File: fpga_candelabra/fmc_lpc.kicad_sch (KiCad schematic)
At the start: 2 parts, among them J5 Samtec_ASP-134603-01

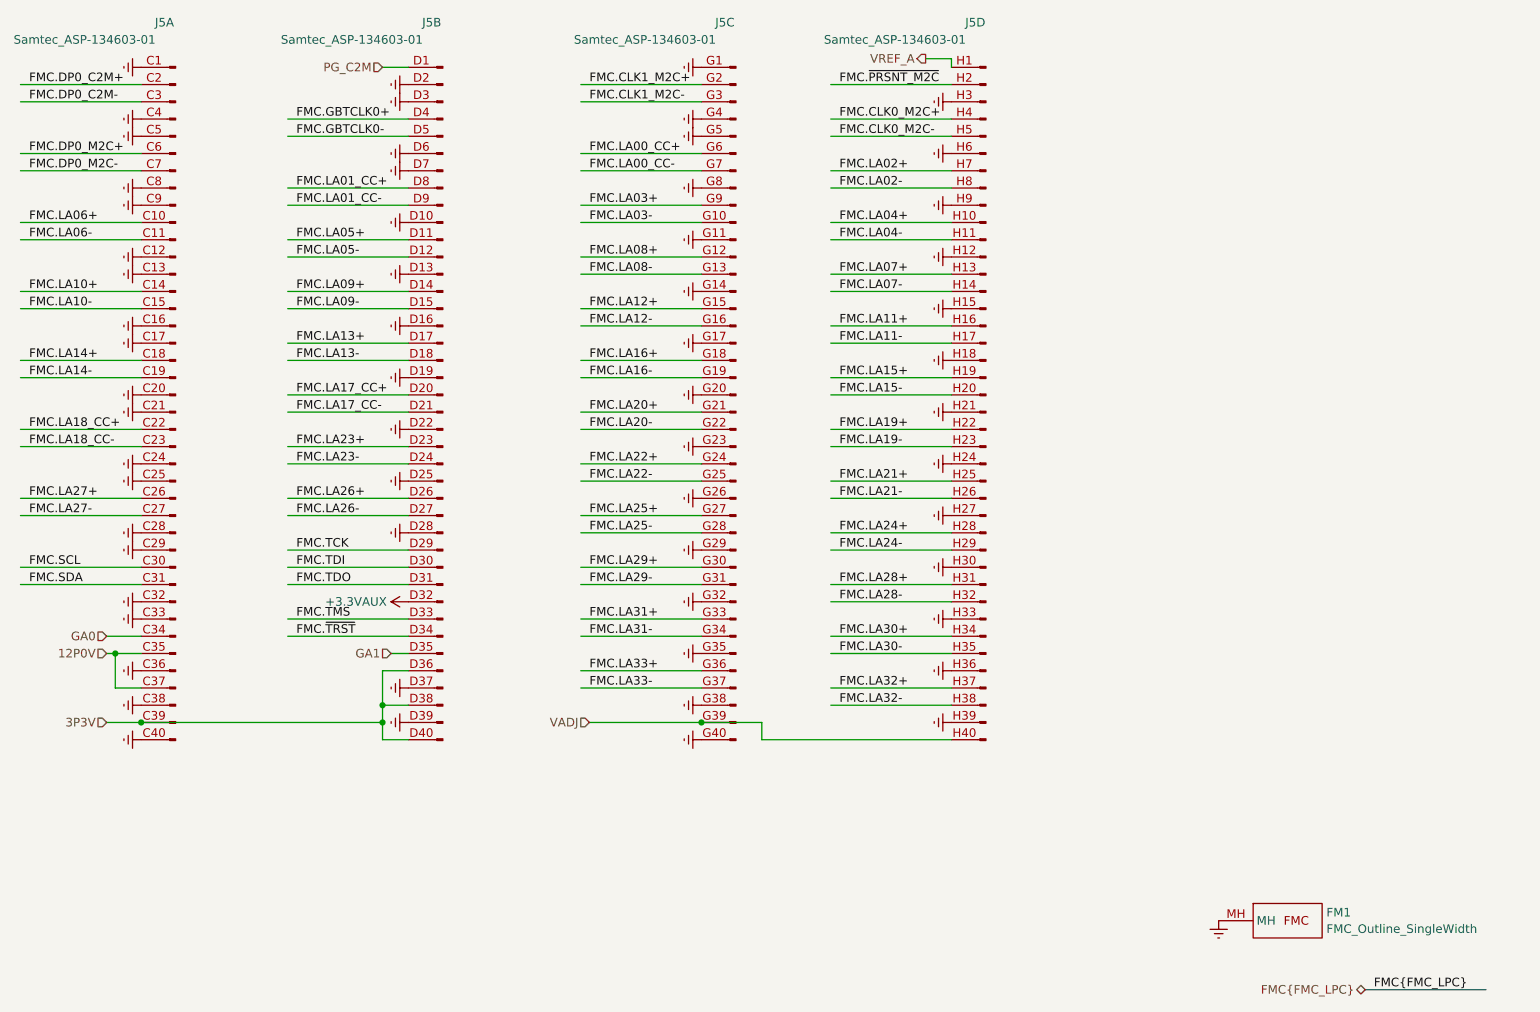
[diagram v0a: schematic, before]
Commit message: fpga_candelabra: sch & layout v0.5, pass basic ERC & DRC
Signed-off-by: Yichuan Gao <gaoyichuan000@gmail.com>
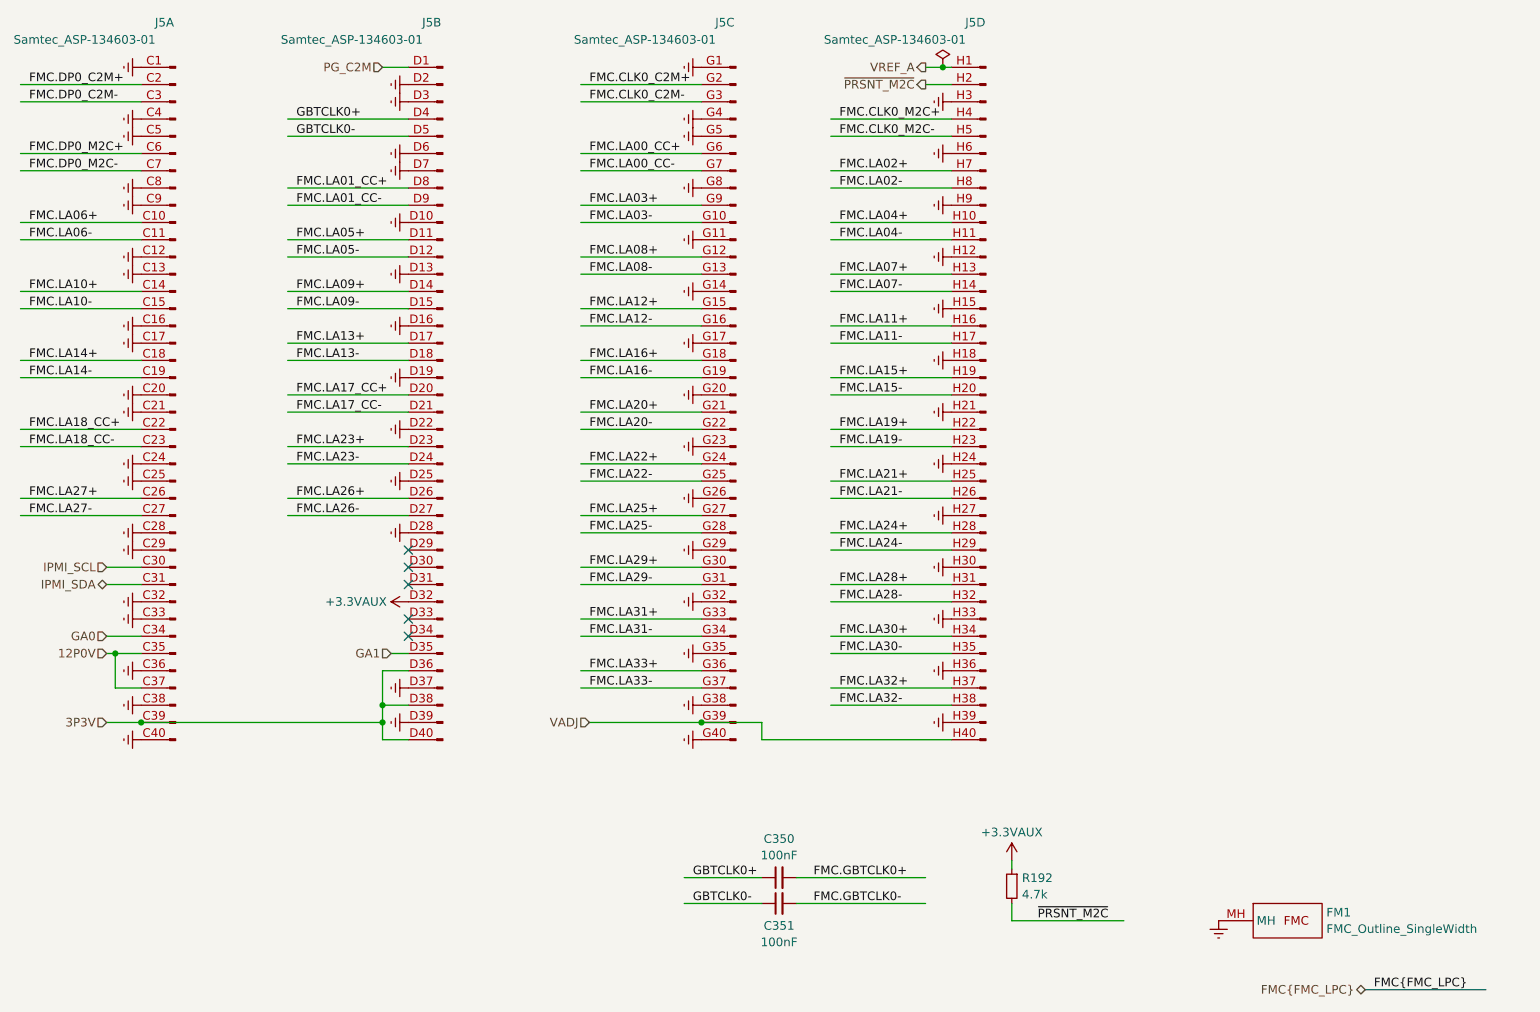
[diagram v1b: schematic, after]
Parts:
- added C350, C351: 100nF, Capacitor_SMD:C_0402_1005Metric, symbol Device:C_Small
- added R192: 4.7k, Resistor_SMD:R_0402_1005Metric, symbol Device:R_Small
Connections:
- net +3.3VAUX: now also R192.1
- net FMC.GBTCLK0+: now also C350.2; no longer J5.D4 (Pin_4)
- net FMC.GBTCLK0-: now also C351.2; no longer J5.D5 (Pin_5)
- net FMC.CLK1_M2C+ renamed FMC.CLK0_C2M+
- net FMC.CLK1_M2C- renamed FMC.CLK0_C2M-
- net FMC.SCL renamed IPMI_SCL
- net FMC.SDA renamed IPMI_SDA
- net FMC.TCK: no longer names the net of J5.D29 (Pin_29)
- net FMC.TDI: no longer names the net of J5.D30 (Pin_30)
- net FMC.TDO: no longer names the net of J5.D31 (Pin_31)
- net FMC.TMS: no longer names the net of J5.D33 (Pin_33)
- net FMC.~{PRSNT_M2C} renamed ~{PRSNT_M2C}
- net ~{PRSNT_M2C}: now also R192.2
- net FMC.~{TRST}: no longer names the net of J5.D34 (Pin_34)
- new net GBTCLK0+: C350.1, J5.D4 (Pin_4)
- new net GBTCLK0-: C351.1, J5.D5 (Pin_5)
- no-connect marks 0 -> 5

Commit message: fpga_candelabra: add author & rev to schematics
Signed-off-by: Yichuan Gao <gaoyichuan000@gmail.com>
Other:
- company: (none) -> CHIPS Alliance
- title: (none) -> FMC LPC Connector
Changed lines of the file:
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@@
 	(generator_version "8.0")
 	(paper "A4")
+	(title_block
+		(title "FMC LPC Connector")
+		(date "2025-02-05")
+		(rev "0.2.0")
+		(company "CHIPS Alliance")
+		(comment 1 "Yichuan Gao")
+		(comment 2 "Yichuan Gao")
+	)
 	(junction
 		(at 165.1 121.92)

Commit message: fpga_candelabra: update to kicad 9.0
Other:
- company: CHIPS Alliance -> Sipeed
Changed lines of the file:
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@@
 (kicad_sch
-	(version 20231120)
+	(version 20250114)
 	(generator "eeschema")
-	(generator_version "8.0")
+	(generator_version "9.0")
 	(paper "A4")
 	(title_block
@@
 		(date "2025-02-05")
 		(rev "0.2.0")
-		(company "CHIPS Alliance")
-		(comment 1 "Yichuan Gao")
-		(comment 2 "Yichuan Gao")
+		(company "Sipeed")
+		(comment 1 "Sipeed")
+		(comment 2 "Sipeed")
 	)
 	(junction
@@
 			"UicAAAAAAAAAAAAAAAAAAACCI868AwAAAAAAAAAAAAAAAAAAAKHHpE4AAAAAAAAAAAAAAAAAAIAI"
 			"wKROAAAAAAAAAAAAAAAAAACACMCkTgAAAAAAAAAAAAAAAAAAgAjApE4AAAAAAAAAAAAAAAAAAIAI"
-			"8H9pe8dzwJBN5gAAAABJRU5ErkJggg=="
+			"8H9pe8dzwJBN5gAAAABJRU5ErkJgggBzAAAAQgAAAFcAAABWAAAAWQAAAHUAAAA4AAAAcAAAAFMA"
+			"AABZAAAALwAAADQAAABNAAAARAAAAG0AAAA1AAAAWgAAAHoAAAA2AAAAWQAAAHoAAABPAAAALwAA"
+			"AEIAAABFAAAAegAAAEMAAABRAAAAUwAAAE8AAABQAAAALwAAADQAAABWAAAANAAAAEcAAABKAAAA"
+			"bQAAAFAAAABDAAAAeQAAAEUAAABzAAAASgAAAGMAAABjAAAATAAAADgAAABTAAAAagAAAEoAAABy"
+			"AAAARQAAADUAAABZAAAAcAAAAEcAAABQAAAASAAAAGoAAABzAAAAYgAAAHkAAAAxAAAAcQAAADMA"
+			"AAA1AAAAWAAAADAAAABoAAAAawAAAEgAAABaAAAAZwAAAHEAAABWAAAAcQAAAHkAAABJAAAAdAAA"
+			"ADcAAABkAAAAdAAAAHQAAABoAAAAcwAAAFIAAAB0AAAAcQAAAGYAAABUAAAANgAAAFoAAABnAAAA"
+			"OAAAAGUAAABUAAAASgAAAHUAAABiAAAAbQAAADQAAABBAAAALwAAAFAAAABEAAAARAAAAEQAAAAx"
+			"AAAAeQAAACsAAABmAAAARgAAAG4AAABWAAAAUwAAAHQAAABHAAAAMwAAAGIAAAAxAAAAOQAAAGoA"
+			"AABlAAAAZQAAAEgAAABDAAAAaAAAAGEAAABTAAAAbQAAAFoAAABtAAAAOAAAAHoAAABtAAAAWgAA"
+			"AC8AAABnAAAANAAAAEcAAABBAAAAUwAAAEUAAABwAAAAVAAAAFYAAABrAAAAOQAAAHEAAAAyAAAA"
+			"YgAAAFUAAAB1AAAAWgAAAE0AAABzAAAAcQAAAGIAAAAxAAAAVQAAAEsAAABJAAAAaAAAAHkAAAB2"
+			"AAAASQAAAEcAAABBAAAAVQAAAFoAAABwAAAAMAAAAEoAAABZAAAAMgAAADgAAABDAAAAUAAAAEIA"
+			"AAArAAAATAAAAGkAAABwAAAAbQAAAHoAAABCAAAAdgAAAFAAAABLAAAAcgAAAGwAAABlAAAAegAA"
+			"AGYAAAB1AAAAbAAAAC8AAABWAAAAdwAAAHIAAABaAAAAMAAAAE8AAABoAAAAMAAAAHoAAABWAAAA"
+			"cwAAADMAAABBAAAAMwAAAFYAAABQAAAAWgAAAHoAAABqAAAAbAAAAGcAAABVAAAAZwAAAEEAAABY"
+			"AAAAVAAAADEAAAAxAAAAVQAAAHQAAABTAAAAcQAAAGEAAABaAAAAYgAAAE8AAABXAAAAYwAAAGUA"
+			"AAB1AAAASwAAAGsAAABwAAAARAAAAFcAAAB2AAAARwAAAE4AAAB6AAAAbgAAAHEAAAByAAAALwAA"
+			"AGwAAABLAAAAcQAAAEYAAABFAAAATA=="
 		)
 	)
